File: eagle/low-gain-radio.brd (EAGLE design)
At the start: 99 x 98 mm, 133 parts, among them U1 MKW01Z128, U2 SKY65116, U3 W25Q80DV, U4 LP5907MFX-3.3, U6 LP5907MFX-3.3, U7 LD39200, U8 MAAL-010704, Y1 32MHz

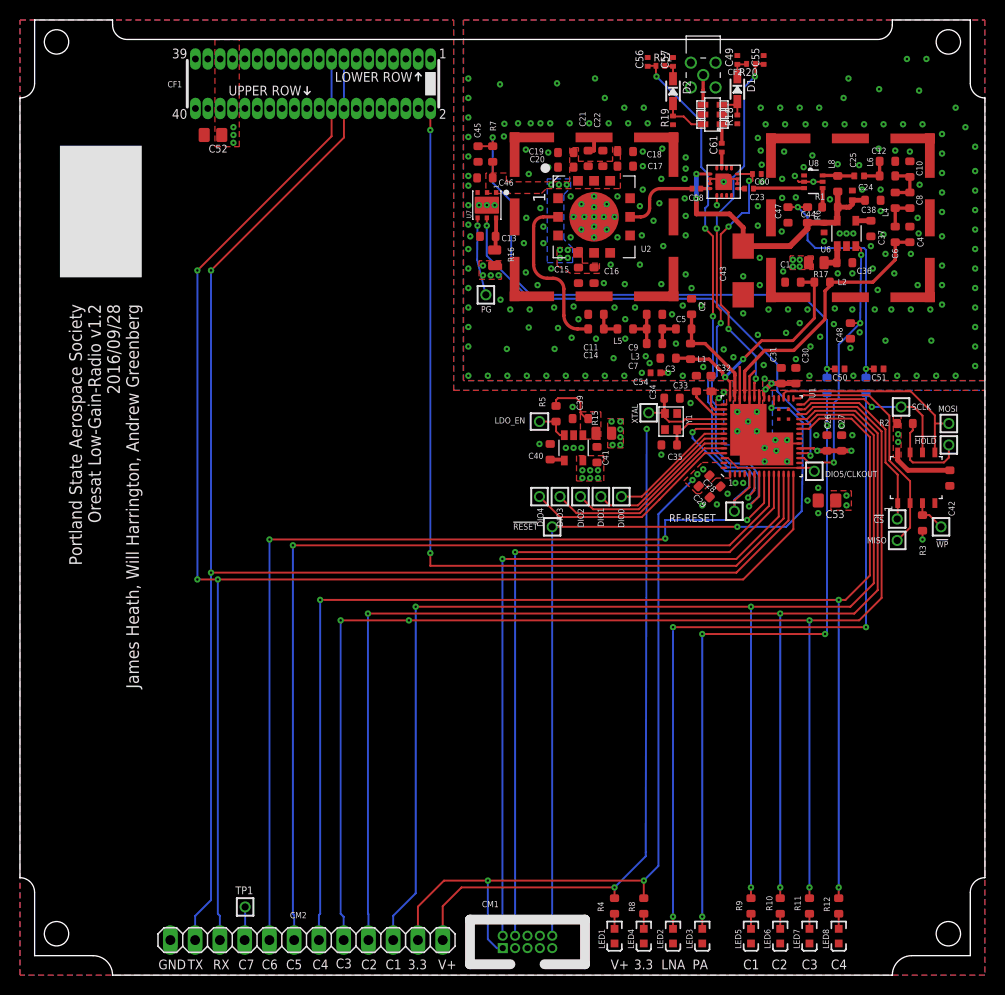
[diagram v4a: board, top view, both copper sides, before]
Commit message: Newest v0.4 card outline and fixed annoying via and changed text to v2
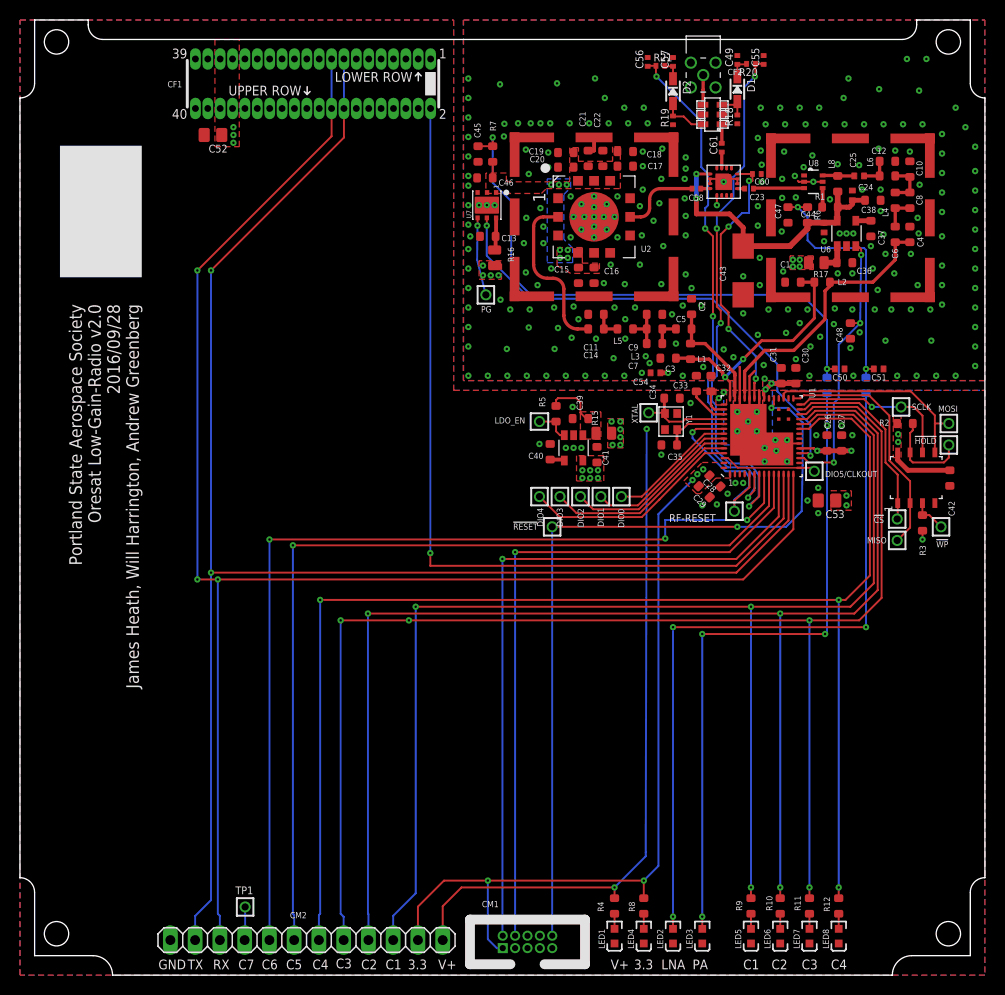
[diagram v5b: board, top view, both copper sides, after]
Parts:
- U$35: device oresat-eagle:ORESAT-CARD-RF-V0.4 -> oresat-eagle:ORESAT-CARD-V0.4
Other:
- outline, holes or cut-outs redrawn
- board text added: "Portland State Aerospace Society Oresat Low-Gain-Radio v2.0 2016/09/28 James Heath, Will Harrington, Andrew Greenberg"
- board text removed: "Portland State Aerospace Society Oresat Low-Gain-Radio v1.2 2016/09/28 James Heath, Will Harrington, Andrew Greenberg"
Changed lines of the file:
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@@
 <?xml version="1.0" encoding="utf-8"?>
 <!DOCTYPE eagle SYSTEM "eagle.dtd">
-<eagle version="7.3.0">
+<eagle version="7.5.0">
 <drawing>
 <settings>
@@
 <layer number="23" name="tOrigins" color="15" fill="1" visible="yes" active="yes"/>
 <layer number="24" name="bOrigins" color="15" fill="1" visible="yes" active="yes"/>
-<layer number="25" name="tNames" color="7" fill="1" visible="yes" active="yes"/>
-<layer number="26" name="bNames" color="7" fill="1" visible="yes" active="yes"/>
+<layer number="25" name="tNames" color="7" fill="1" visible="no" active="yes"/>
+<layer number="26" name="bNames" color="7" fill="1" visible="no" active="yes"/>
 <layer number="27" name="tValues" color="7" fill="1" visible="no" active="yes"/>
 <layer number="28" name="bValues" color="7" fill="1" visible="no" active="yes"/>
-<layer number="29" name="tStop" color="7" fill="3" visible="no" active="yes"/>
-<layer number="30" name="bStop" color="7" fill="6" visible="no" active="yes"/>
+<layer number="29" name="tStop" color="7" fill="3" visible="yes" active="yes"/>
+<layer number="30" name="bStop" color="7" fill="6" visible="yes" active="yes"/>
 <layer number="31" name="tCream" color="7" fill="4" visible="no" active="yes"/>
 <layer number="32" name="bCream" color="7" fill="5" visible="no" active="yes"/>
@@
 <layer number="44" name="Drills" color="7" fill="1" visible="no" active="yes"/>
 <layer number="45" name="Holes" color="7" fill="1" visible="no" active="yes"/>
-<layer number="46" name="Milling" color="3" fill="1" visible="no" active="yes"/>
-<layer number="47" name="Measures" color="7" fill="1" visible="yes" active="yes"/>
+<layer number="46" name="Milling" color="3" fill="1" visible="yes" active="yes"/>
+<layer number="47" name="Measures" color="7" fill="1" visible="no" active="yes"/>
 <layer number="48" name="Document" color="7" fill="1" visible="yes" active="yes"/>
-<layer number="49" name="Reference" color="7" fill="1" visible="yes" active="yes"/>
+<layer number="49" name="Reference" color="7" fill="1" visible="no" active="yes"/>
 <layer number="50" name="dxf" color="7" fill="1" visible="no" active="no"/>
 <layer number="51" name="tDocu" color="7" fill="1" visible="yes" active="yes"/>
@@
 <text x="14.2" y="0.6" size="1" layer="21" font="vector" ratio="20">GND</text>
 <text x="5.05" y="68.85" size="1.3" layer="21" font="vector" ratio="15" rot="R270">Portland State Aerospace Society
-Oresat Low-Gain-Radio v1.2
+Oresat Low-Gain-Radio v2.0
 2016/09/28
 James Heath, Will Harrington, Andrew Greenberg</text>
@@
 </element>
 <element name="CF2" library="oresat-eagle" package="CON-MMCX-F-MOLEX-0734151001" value="CON-MMCX-F-MOLEX-0734151001" x="70.1" y="92.35"/>
-<element name="U$35" library="oresat-eagle" package="ORESAT-CARD-RF-V0.4" value="" x="0" y="0"/>
 <element name="RF-RESET" library="Tova" package="2MM-TEST-POINT" value="TEST-POINT" x="73.3" y="47.6" smashed="yes">
 <attribute name="NAME" x="66.6" y="46.5" size="0.8" layer="25" font="vector" ratio="20"/>
@@
 <attribute name="MPN" value="CBR04C101F3GAC" x="72" y="84.9" size="1.778" layer="27" rot="R90" display="off"/>
 </element>
+<element name="U$35" library="oresat-eagle" package="ORESAT-CARD-V0.4" value="" x="0" y="0"/>
 </elements>
 <signals>
@@
 <wire x1="42.1" y1="42" x2="42.1" y2="43.3" width="0.2" layer="1"/>
 <via x="42.1" y="43.3" extent="1-16" drill="0.254"/>
-<wire x1="42.1" y1="43.3" x2="42.1" y2="86.7" width="0.2" layer="16"/>
-<via x="42.1" y="86.7" extent="1-16" drill="0.254"/>
+<wire x1="42.1" y1="43.3" x2="42.1" y2="88.92" width="0.2" layer="16"/>
 <contactref element="CF1" pad="P$2"/>
-<wire x1="42.1" y1="86.7" x2="42.1" y2="88.92" width="0.2" layer="1"/>
 <wire x1="42.1" y1="88.92" x2="42.13" y2="88.92" width="0.2" layer="1"/>
+<via x="42.1" y="88.92" extent="1-16" drill="0.6" shape="square"/>
 </signal>
 <signal name="N$5">

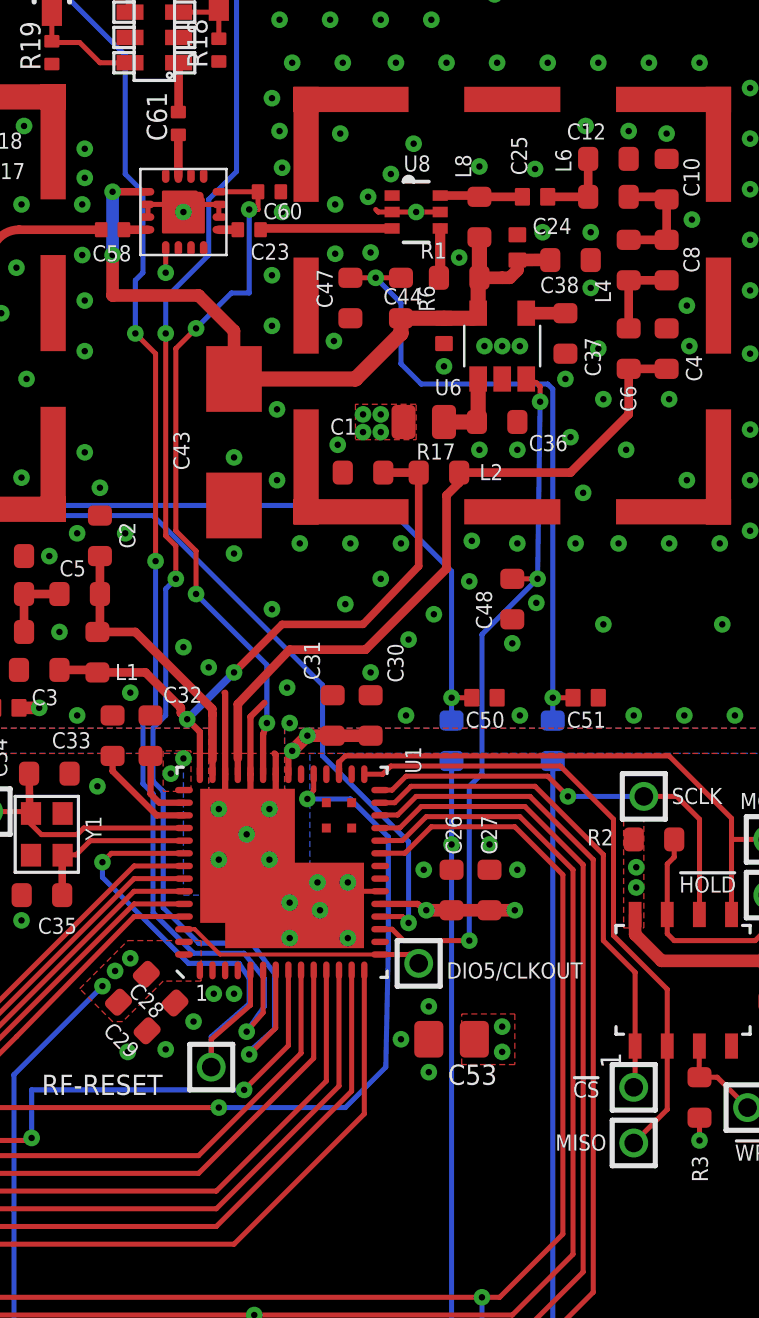
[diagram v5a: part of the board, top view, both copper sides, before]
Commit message: added test points to PTB17, PTB2 and placed on PCB layout...also cleared a few stupid DRC errors on the PCB layout
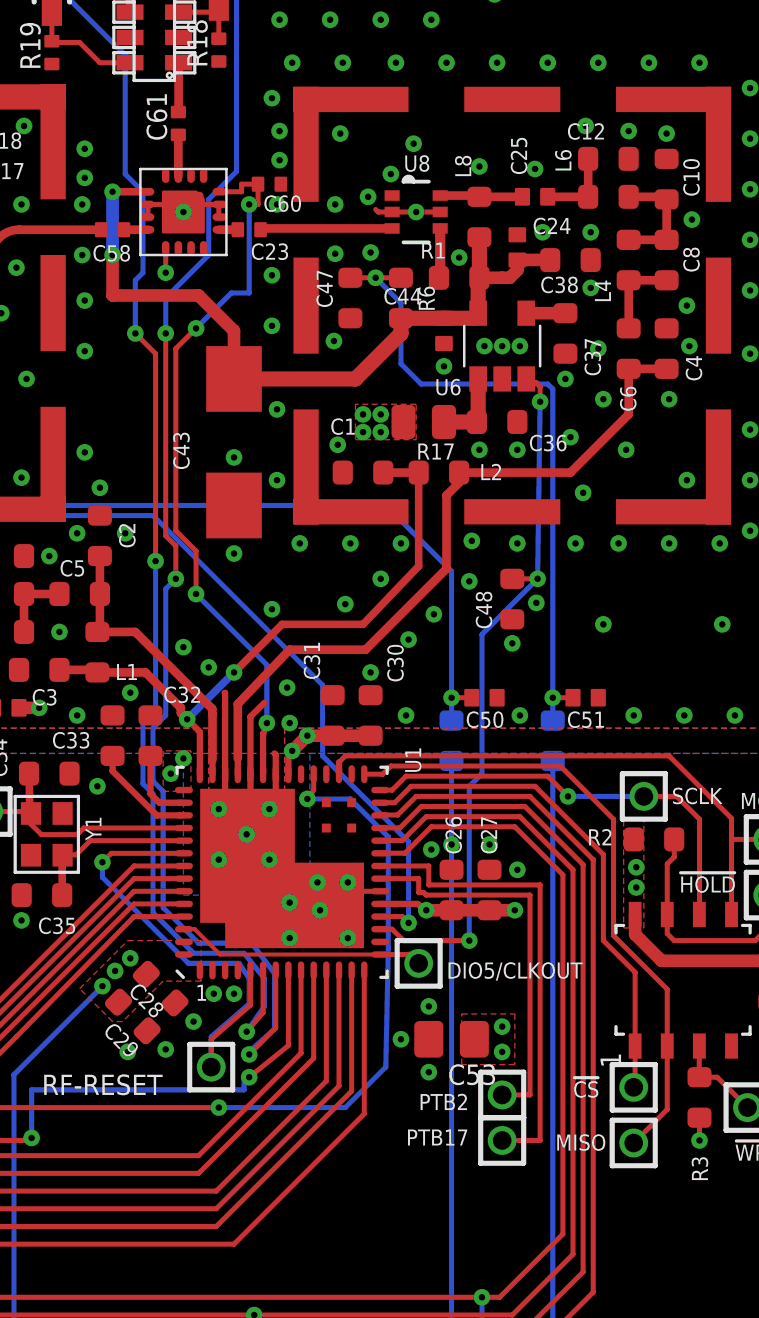
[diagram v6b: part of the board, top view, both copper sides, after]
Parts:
- added PTB17, PTB2: TEST-POINT, Tova:2MM-TEST-POINT
- moved C60 0.30 mm to (75.6, 82.5)
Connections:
- new net PTB17: PTB17.1, U1.22
- new net PTB2: PTB2.1, U1.21
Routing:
- net PTB17: track 0.00 -> 18.7 mm
- net PTB2: track 0.00 -> 15.5 mm
- net RXTX: track 28.0 -> 28.6 mm
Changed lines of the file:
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@@
 <?xml version="1.0" encoding="utf-8"?>
 <!DOCTYPE eagle SYSTEM "eagle.dtd">
-<eagle version="7.5.0">
+<eagle version="7.3.0">
 <drawing>
 <settings>
@@
 <setting verticaltext="up"/>
 </settings>
-<grid distance="0.1" unitdist="mm" unit="mil" style="lines" multiple="1" display="yes" altdistance="0.025" altunitdist="inch" altunit="inch"/>
+<grid distance="0.1" unitdist="mm" unit="mm" style="lines" multiple="1" display="yes" altdistance="0.025" altunitdist="inch" altunit="inch"/>
 <layers>
 <layer number="1" name="Top" color="4" fill="1" visible="yes" active="yes"/>
@@
 <layer number="13" name="Route13" color="4" fill="5" visible="no" active="no"/>
 <layer number="14" name="Route14" color="1" fill="6" visible="no" active="no"/>
-<layer number="15" name="Route15" color="14" fill="1" visible="no" active="yes"/>
+<layer number="15" name="Route15" color="14" fill="1" visible="yes" active="yes"/>
 <layer number="16" name="Bottom" color="1" fill="1" visible="yes" active="yes"/>
 <layer number="17" name="Pads" color="2" fill="1" visible="yes" active="yes"/>
@@
 <layer number="23" name="tOrigins" color="15" fill="1" visible="yes" active="yes"/>
 <layer number="24" name="bOrigins" color="15" fill="1" visible="yes" active="yes"/>
-<layer number="25" name="tNames" color="7" fill="1" visible="no" active="yes"/>
+<layer number="25" name="tNames" color="7" fill="1" visible="yes" active="yes"/>
 <layer number="26" name="bNames" color="7" fill="1" visible="no" active="yes"/>
 <layer number="27" name="tValues" color="7" fill="1" visible="no" active="yes"/>
@@
 <attribute name="NAME" x="74.8" y="80.7" size="0.2" layer="33" ratio="15" rot="R180" align="center"/>
 </element>
-<element name="C60" library="low-gain-radio" package=".0402-C-NOSILK" value="100pF" x="75.6" y="82.2" smashed="yes" rot="R180">
-<attribute name="DPN" value="399-11246-2-ND" x="75.6" y="82.2" size="1.778" layer="27" rot="R180" display="off"/>
-<attribute name="MFG" value="Kemet" x="75.6" y="82.2" size="1.778" layer="27" rot="R180" display="off"/>
-<attribute name="DIST" value="Digi-Key Inc." x="75.6" y="82.2" size="1.778" layer="27" rot="R180" display="off"/>
-<attribute name="MPN" value="CBR04C101F3GAC" x="75.6" y="82.2" size="1.778" layer="27" rot="R180" display="off"/>
-<attribute name="NAME" x="76.9" y="81.75" size="0.635" layer="25" font="vector" ratio="20" rot="R180"/>
-<attribute name="VALUE" x="76.3" y="83.45" size="0.8" layer="27" font="vector" ratio="15" rot="R180"/>
-<attribute name="NAME" x="75.6" y="82.2" size="0.2" layer="33" ratio="15" rot="R180" align="center"/>
+<element name="C60" library="low-gain-radio" package=".0402-C-NOSILK" value="100pF" x="75.6" y="82.5" smashed="yes" rot="R180">
+<attribute name="DPN" value="399-11246-2-ND" x="75.6" y="82.5" size="1.778" layer="27" rot="R180" display="off"/>
+<attribute name="MFG" value="Kemet" x="75.6" y="82.5" size="1.778" layer="27" rot="R180" display="off"/>
+<attribute name="DIST" value="Digi-Key Inc." x="75.6" y="82.5" size="1.778" layer="27" rot="R180" display="off"/>
+<attribute name="MPN" value="CBR04C101F3GAC" x="75.6" y="82.5" size="1.778" layer="27" rot="R180" display="off"/>
+<attribute name="NAME" x="76.9" y="82.05" size="0.635" layer="25" font="vector" ratio="20" rot="R180"/>
+<attribute name="VALUE" x="76.3" y="83.75" size="0.8" layer="27" font="vector" ratio="15" rot="R180"/>
+<attribute name="NAME" x="75.6" y="82.5" size="0.2" layer="33" ratio="15" rot="R180" align="center"/>
 </element>
 <element name="C61" library="low-gain-radio" package=".0402-C-NOSILK" value="100pF" x="72" y="84.9" rot="R90">
@@
 </element>
 <element name="U$35" library="oresat-eagle" package="ORESAT-CARD-V0.4" value="" x="0" y="0"/>
+<element name="PTB2" library="Tova" package="2MM-TEST-POINT" value="TEST-POINT" x="84.8" y="46.5" smashed="yes">
+<attribute name="NAME" x="81.5" y="45.9" size="0.635" layer="25" font="vector" ratio="20"/>
+</element>
+<element name="PTB17" library="Tova" package="2MM-TEST-POINT" value="TEST-POINT" x="84.8" y="44.7" smashed="yes">
+<attribute name="NAME" x="81" y="44.5" size="0.635" layer="25" font="vector" ratio="20"/>
+</element>
 </elements>
 <signals>
@@
 <via x="84.3" y="56.4" extent="1-16" drill="0.254"/>
 <via x="82.8" y="56.4" extent="1-16" drill="0.254"/>
-<via x="81.7" y="55.4" extent="1-16" drill="0.254"/>
+<via x="82" y="56.2" extent="1-16" drill="0.254"/>
 <via x="77.5" y="54.9" extent="1-16" drill="0.254"/>
 <via x="78.7" y="54.9" extent="1-16" drill="0.254"/>
@@
 <via x="73.4" y="50.5" extent="1-16" drill="0.254"/>
 <via x="74.2" y="50.5" extent="1-16" drill="0.254"/>
+<wire x1="77.7" y1="53.8" x2="77.6" y2="53.8" width="0" layer="19" extent="1-1"/>
 </signal>
 <signal name="SWD_DIO">
@@
 <contactref element="U$49" pad="VC"/>
 <contactref element="C60" pad="2"/>
-<wire x1="75.15" y1="82.2" x2="73.6" y2="82.2" width="0.2" layer="1"/>
+<wire x1="75.15" y1="82.5" x2="74.5" y2="82.5" width="0.2" layer="1"/>
+<wire x1="74.5" y1="82.5" x2="74.5" y2="82.2" width="0.2" layer="1"/>
+<wire x1="74.5" y1="82.2" x2="73.6" y2="82.2" width="0.2" layer="1"/>
 <wire x1="74.1" y1="78.2" x2="74.8" y2="78.2" width="0.2" layer="16"/>
-<wire x1="74.8" y1="78.2" x2="74.8" y2="81.5" width="0.2" layer="16"/>
-<via x="74.8" y="81.5" extent="1-16" drill="0.254"/>
-<wire x1="74.8" y1="81.5" x2="75.15" y2="81.5" width="0.2" layer="1"/>
-<wire x1="75.15" y1="81.5" x2="75.15" y2="82.2" width="0.2" layer="1"/>
+<wire x1="74.8" y1="78.2" x2="74.8" y2="81.7" width="0.2" layer="16"/>
+<via x="74.8" y="81.7" extent="1-16" drill="0.254"/>
+<wire x1="74.8" y1="81.7" x2="75.15" y2="81.7" width="0.2" layer="1"/>
+<wire x1="75.15" y1="81.7" x2="75.15" y2="82.5" width="0.2" layer="1"/>
 </signal>
 <signal name="VR_PA">
@@
 <via x="68.2" y="81.7" extent="1-16" drill="0.254" diameter="0.245"/>
 <via x="68.3" y="83.9" extent="1-16" drill="0.254" diameter="0.245"/>
-<via x="76.1" y="81.4" extent="1-16" drill="0.254" diameter="0.245"/>
+<via x="75.9" y="81.7" extent="1-16" drill="0.254" diameter="0.245"/>
 <via x="75.7" y="85.9" extent="1-16" drill="0.254" diameter="0.245"/>
 <via x="76" y="84.6" extent="1-16" drill="0.254" diameter="0.245"/>
@@
 <via x="74.2" y="71.7" extent="1-16" drill="0.254" diameter="0.245"/>
 <via x="74.2" y="67.9" extent="1-16" drill="0.254" diameter="0.245"/>
-<via x="76.1" y="83.15" extent="1-16" drill="0.254" diameter="0.245"/>
+<via x="76" y="83.45" extent="1-16" drill="0.254" diameter="0.245"/>
 <via x="68.3" y="82.75" extent="1-16" drill="0.254" diameter="0.245"/>
 <via x="78.3" y="72.2" extent="1-16" drill="0.254" diameter="0.245"/>
@@
 <contactref element="CM2" pad="8"/>
 <wire x1="76.35" y1="51.4222" x2="76.35" y2="48.45" width="0.2" layer="1"/>
-<wire x1="76.35" y1="48.45" x2="74.6" y2="46.7" width="0.2" layer="1"/>
-<via x="74.6" y="46.7" extent="1-16" drill="0.254"/>
+<wire x1="76.35" y1="48.45" x2="74.8" y2="47.2" width="0.2" layer="1"/>
+<via x="74.8" y="47.2" extent="1-16" drill="0.254"/>
+<wire x1="74.8" y1="47.2" x2="74.6" y2="47.2" width="0.2" layer="16"/>
+<wire x1="74.6" y1="47.2" x2="74.6" y2="46.7" width="0.2" layer="16"/>
 <wire x1="74.6" y1="46.7" x2="66.2" y2="46.7" width="0.2" layer="16"/>
 <wire x1="66.2" y1="46.7" x2="66.2" y2="44.8" width="0.2" layer="16"/>
@@
 <wire x1="25.6" y1="3.6" x2="25.59" y2="3.6" width="0.2" layer="16"/>
 </signal>
+<signal name="PTB2">
+<contactref element="U1" pad="21"/>
+<contactref element="PTB2" pad="1"/>
+<wire x1="79.9778" y1="55.05" x2="81.5" y2="55.05" width="0.2" layer="1"/>
+<wire x1="81.5" y1="55.05" x2="81.5" y2="54.5" width="0.2" layer="1"/>
+<wire x1="81.5" y1="54.5" x2="81.7" y2="54.5" width="0.2" layer="1"/>
+<wire x1="81.7" y1="54.5" x2="81.8" y2="54.4" width="0.2" layer="1"/>
+<wire x1="81.8" y1="54.4" x2="85.9" y2="54.4" width="0.2" layer="1"/>
+<wire x1="85.9" y1="54.4" x2="85.9" y2="46.5" width="0.2" layer="1"/>
+<wire x1="84.8" y1="46.5" x2="85.9" y2="46.5" width="0.2" layer="1"/>
+</signal>
+<signal name="PTB17">
+<contactref element="U1" pad="22"/>
+<contactref element="PTB17" pad="1"/>
+<wire x1="79.9778" y1="55.55" x2="81.9" y2="55.55" width="0.2" layer="1"/>
+<wire x1="81.9" y1="55.55" x2="81.9" y2="54.8" width="0.2" layer="1"/>
+<wire x1="81.9" y1="54.8" x2="86.3" y2="54.8" width="0.2" layer="1"/>
+<wire x1="86.3" y1="54.8" x2="86.3" y2="44.7" width="0.2" layer="1"/>
+<wire x1="86.3" y1="44.7" x2="84.8" y2="44.7" width="0.2" layer="1"/>
+</signal>
 </signals>
